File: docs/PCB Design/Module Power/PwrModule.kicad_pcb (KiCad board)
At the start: 4 copper layers, 25.9 x 62.3 mm, 4 parts, among them J11 Conn_02x05_Top_Bottom, J14 Conn_02x04_Counter_Clockwise

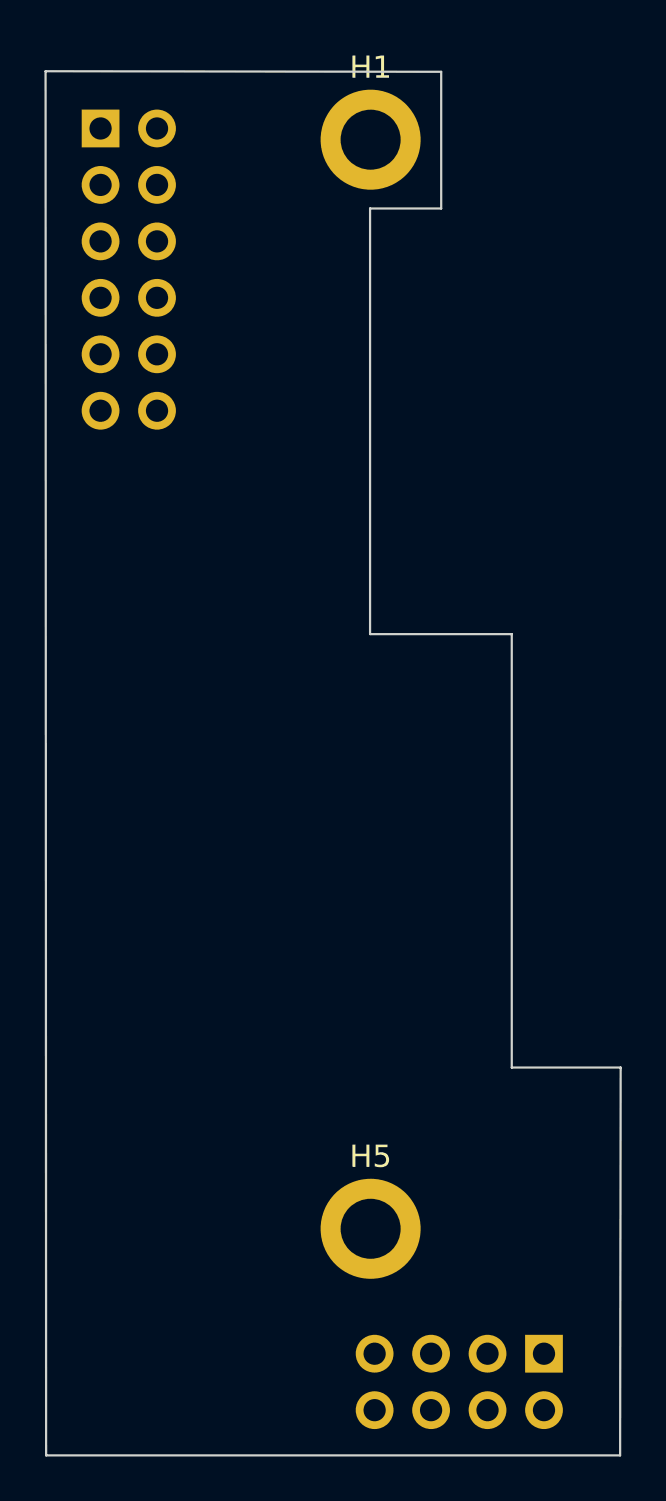
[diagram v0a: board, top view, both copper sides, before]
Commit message: module power 1.0 module bypass 1.1
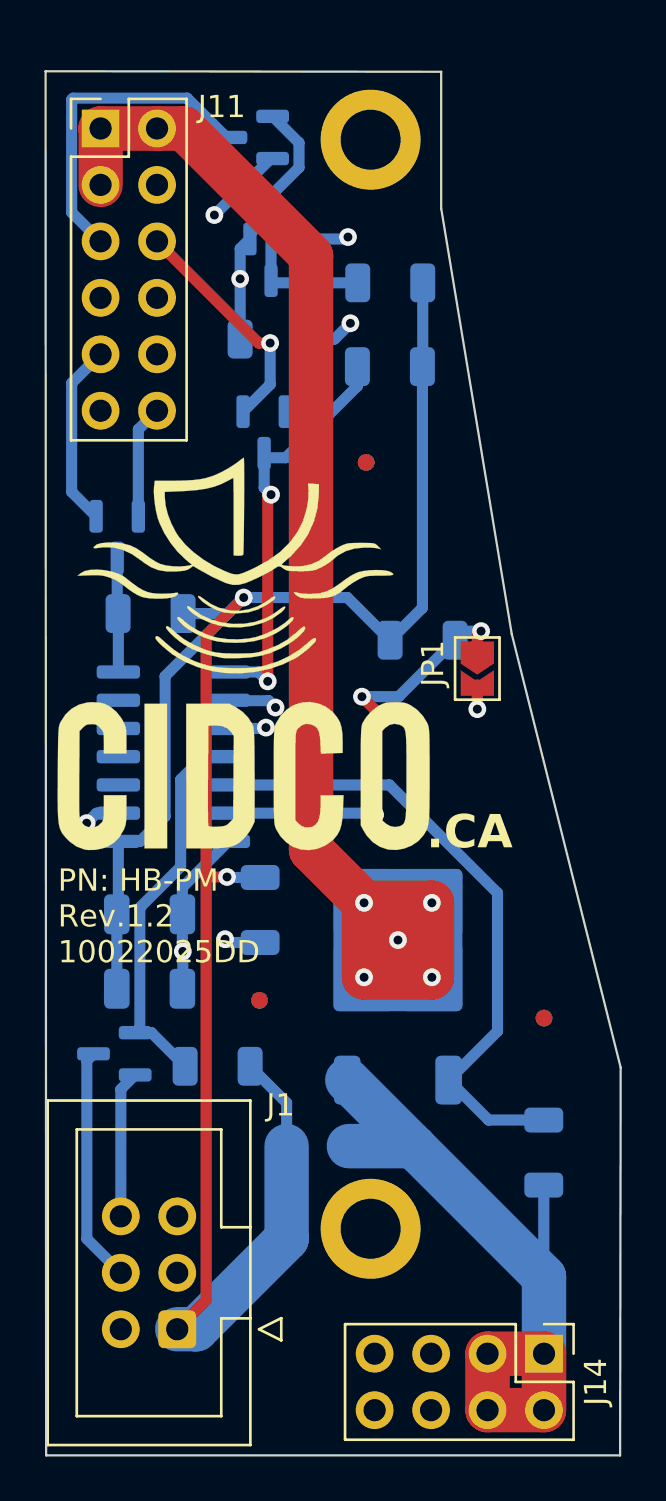
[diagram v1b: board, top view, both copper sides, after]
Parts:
- added C1: 1uf, Capacitor_SMD:C_1206_3216Metric, B.Cu at (106.3, 78.3)
- added C2: 0.1uf, Capacitor_SMD:C_1206_3216Metric, B.Cu at (106.3, 81.7)
- added F1: Fuse, Fuse:Fuse_1206_3216Metric, B.Cu at (113.8, 88.8)
- added FID1: Fiducial, Fiducial:Fiducial_0.75mm_Mask2.25mm, B.Cu at (124.0, 83.0)
- added FID2: Fiducial, Fiducial:Fiducial_0.75mm_Mask2.25mm, F.Cu at (124.0, 83.0)
- added FID3: Fiducial, Fiducial:Fiducial_0.75mm_Mask2.25mm, B.Cu at (116.0, 58.0)
- added FID4: Fiducial, Fiducial:Fiducial_0.75mm_Mask2.25mm, F.Cu at (116.0, 58.0)
- added FID5: Fiducial, Fiducial:Fiducial_0.75mm_Mask2.25mm, B.Cu at (111.2, 82.2)
- added FID6: Fiducial, Fiducial:Fiducial_0.75mm_Mask2.25mm, F.Cu at (111.2, 82.2)
- added J1: Conn_02x03_Top_Bottom, Connector_IDC:IDC-Header_2x03_P2.54mm_Vertical, F.Cu at (107.5, 97.0)
- added JP1: SolderJumper_2_Open, Jumper:SolderJumper-2_P1.3mm_Open_TrianglePad1.0x1.5mm, F.Cu at (121.0, 67.3)
- added Q1: 2N7002, Package_TO_SOT_SMD:SOT-23, B.Cu at (104.7, 84.6)
- added Q2: DMP3010LK3Q-13, Package_TO_SOT_SMD:TO-252-2, B.Cu at (117.4, 80.8)
- added Q3: 2N7002, Package_TO_SOT_SMD:SOT-23, B.Cu at (110.9, 43.4)
- added Q4: 2N7002, Package_TO_SOT_SMD:SOT-23, B.Cu at (111.7, 48.9)
- added Q5: 2N7002, Package_TO_SOT_SMD:SOT-23, B.Cu at (111.4, 56.7)
- added Q6: 2N7002, Package_TO_SOT_SMD:SOT-23, B.Cu at (104.8, 61.4)
- added R1: 1k, Resistor_SMD:R_1206_3216Metric, B.Cu at (109.3, 85.2)
- added R2: 1k, Resistor_SMD:R_1206_3216Metric, B.Cu at (124.0, 89.0)
- added R3: 1k, Resistor_SMD:R_1206_3216Metric, B.Cu at (118.5, 66.0)
- added R4: 1k, Resistor_SMD:R_1206_3216Metric, B.Cu at (117.1, 49.9)
- added R5: 1k, Resistor_SMD:R_1206_3216Metric, B.Cu at (111.8, 52.5)
- added R6: 1k, Resistor_SMD:R_1206_3216Metric, B.Cu at (117.1, 53.7)
- added R7: 1k, Resistor_SMD:R_1206_3216Metric, B.Cu at (106.3, 64.8)
- added R8: 4.7k, Resistor_SMD:R_1206_3216Metric, B.Cu at (111.2, 78.1)
- added U1: ATtiny424-SS, Package_SO:SOIC-14_3.9x8.7mm_P1.27mm, B.Cu at (107.3, 71.2)
- added logo1: LOGO, cidco:logo cidco, F.Cu at (110.7, 66.3)
- J11: footprint Connector_PinSocket_2.54mm:PinSocket_2x06_P2.54mm_Vertical -> Connector_PinHeader_2.54mm:PinHeader_2x06_P2.54mm_Vertical; moved to F.Cu
- J14: footprint Connector_PinSocket_2.54mm:PinSocket_2x04_P2.54mm_Vertical -> Connector_PinHeader_2.54mm:PinHeader_2x04_P2.54mm_Vertical; moved to F.Cu
- turned J11 to 0 degrees
- turned J14 to -90 degrees
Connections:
- net +5P renamed VCC
- J11 pad 4: +5V -> UPDI
- J11 pad 5: Pwr_off -> Net-(J11-Pin_5)
- J11 pad 6: Pwr_mon -> Net-(J11-Pin_6)
- J11 pad 7: unconnected-(J11-Pin_7-Pad7) -> Red
- J11 pad 8: LedB -> Green
- J11 pad 9: GND -> Net-(J11-Pin_9)
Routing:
- net VCC_: track 0.00 -> 99.8 mm, vias 0 -> 2
- net +5V: track 0.00 -> 59.6 mm, vias 0 -> 5
- net Red: track 0.00 -> 48.1 mm
- net Green: track 0.00 -> 45.3 mm
- net VCC: track 0.00 -> 33.3 mm
- net GND: track 0.00 -> 32.5 mm, vias 0 -> 5
- net Signal: track 0.00 -> 31.1 mm, vias 0 -> 2
- net Net-(Q2-G): track 0.00 -> 28.5 mm
- net UPDI: track 0.00 -> 28.2 mm, vias 0 -> 1
- net Pwr_off: track 0.00 -> 27.6 mm, vias 0 -> 2
- net Net-(JP1-A): track 0.00 -> 19.8 mm, vias 0 -> 3
- net Pwr_mon: track 0.00 -> 18.6 mm, vias 0 -> 2
- net Net-(Q1-G): track 0.00 -> 17.7 mm
- net Net-(J11-Pin_5): track 0.00 -> 14.6 mm
- net Net-(Q3-G): track 0.00 -> 12.3 mm
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- added copper zone on In2.Cu, net GND
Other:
- outline, holes or cut-outs redrawn
- board text added: ".CA"
- board text added: "PN: HB-PM Rev.1.2 10022025DD"
